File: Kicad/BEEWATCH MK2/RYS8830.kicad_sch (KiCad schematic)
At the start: 30 parts, among them Q4 BSS138, Q5 BSS138, Q6 BSS138, Q7 BSS138, U6 LTC3549EDCB#TRMPBF, U7 RYS8830

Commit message: Schematic changes
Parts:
- removed Q4: BSS138, Package_TO_SOT_SMD:SOT-23, symbol Transistor_FET:BSS138
- removed R25: 10K, Resistor_SMD:R_0402_1005Metric, symbol Device:R
- removed U6: LTC3549EDCB#TRMPBF, SON50P300X200X80-7N-D, symbol LTC3549EDCB#TRMPBF:LTC3549EDCB#TRMPBF
- added IC1: LTC3549EDCB#TRMPBF, Package_DFN_QFN:DFN-6-1EP_3x2mm_P0.5mm_EP1.65x1.35mm, symbol LTC3549EDCB#TRMPBF:LTC3549EDCB#TRMPBF
- added Q4: DMG6968U, Package_TO_SOT_SMD:SOT-23, symbol Transistor_FET:DMG2302U
- added Q8: DMP1045U-7, Package_TO_SOT_SMD:SOT-23-3, symbol Project_Library:DMP1045U-7
- added R49: 0, Resistor_SMD:R_0402_1005Metric_Pad0.72x0.64mm_HandSolder, symbol Device:R_Small
- added R50: 10K, Resistor_SMD:R_0402_1005Metric_Pad0.72x0.64mm_HandSolder, symbol Device:R
- L3: footprint Inductor_SMD:L_0402_1005Metric -> Inductor_SMD:L_Cenker_CKCS3012
- R24: value K10K -> 10K; footprint Resistor_SMD:R_0402_1005Metric -> Resistor_SMD:R_0402_1005Metric_Pad0.72x0.64mm_HandSolder
- R26, R27, R28, R29, R30, R31, R32, R33, R34, R35, R36, R37, R38, R39, R41: footprint Resistor_SMD:R_0402_1005Metric -> Resistor_SMD:R_0402_1005Metric_Pad0.72x0.64mm_HandSolder
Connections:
- net +1V8: now also R24.2, Q8.2 (S); no longer Q5.1 (G), Q6.1 (G), Q7.1 (G), R31.2, R32.2, R33.2, R41.2, U7.14 (SYSTEM0)
- net +3V3: no longer R24.2
- net GND: now also IC1.2 (GND_1), IC1.4 (MODE), IC1.7 (GND_2), Q4.2 (S), R50.1
- net GNSS_+1.8V: now also IC1.1 (VIN), IC1.5 (RUN)
- net GPS_EN: now also Q4.1 (G), R50.2; no longer R24.1
- net at C28.1, C29.2, L3.2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: now also R49.1; no longer U7.5 (LDO_IN)
- net at L3.1: now also IC1.3 (SW)
- net at C28.2, R26.2, R27.1: now also IC1.6 (VFB)
- new net: R49.2, U7.5 (LDO_IN)
- new net: Q4.3 (D), Q8.1 (G), R24.1
- new net GNSS_+1V8: Q5.1 (G), Q6.1 (G), Q7.1 (G), Q8.3 (D), R31.2, R32.2, R33.2, R41.2, U7.14 (SYSTEM0)

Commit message: GNSS level shifter floating voltage needs to be fix
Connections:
- net GNSS_+1.8V: now also Q5.1 (G), Q6.1 (G), Q7.1 (G), R31.2, R32.2, R33.2, U7.14 (SYSTEM0)
- net GNSS_+1V8: no longer Q5.1 (G), Q6.1 (G), Q7.1 (G), R31.2, R32.2, R33.2, U7.14 (SYSTEM0)

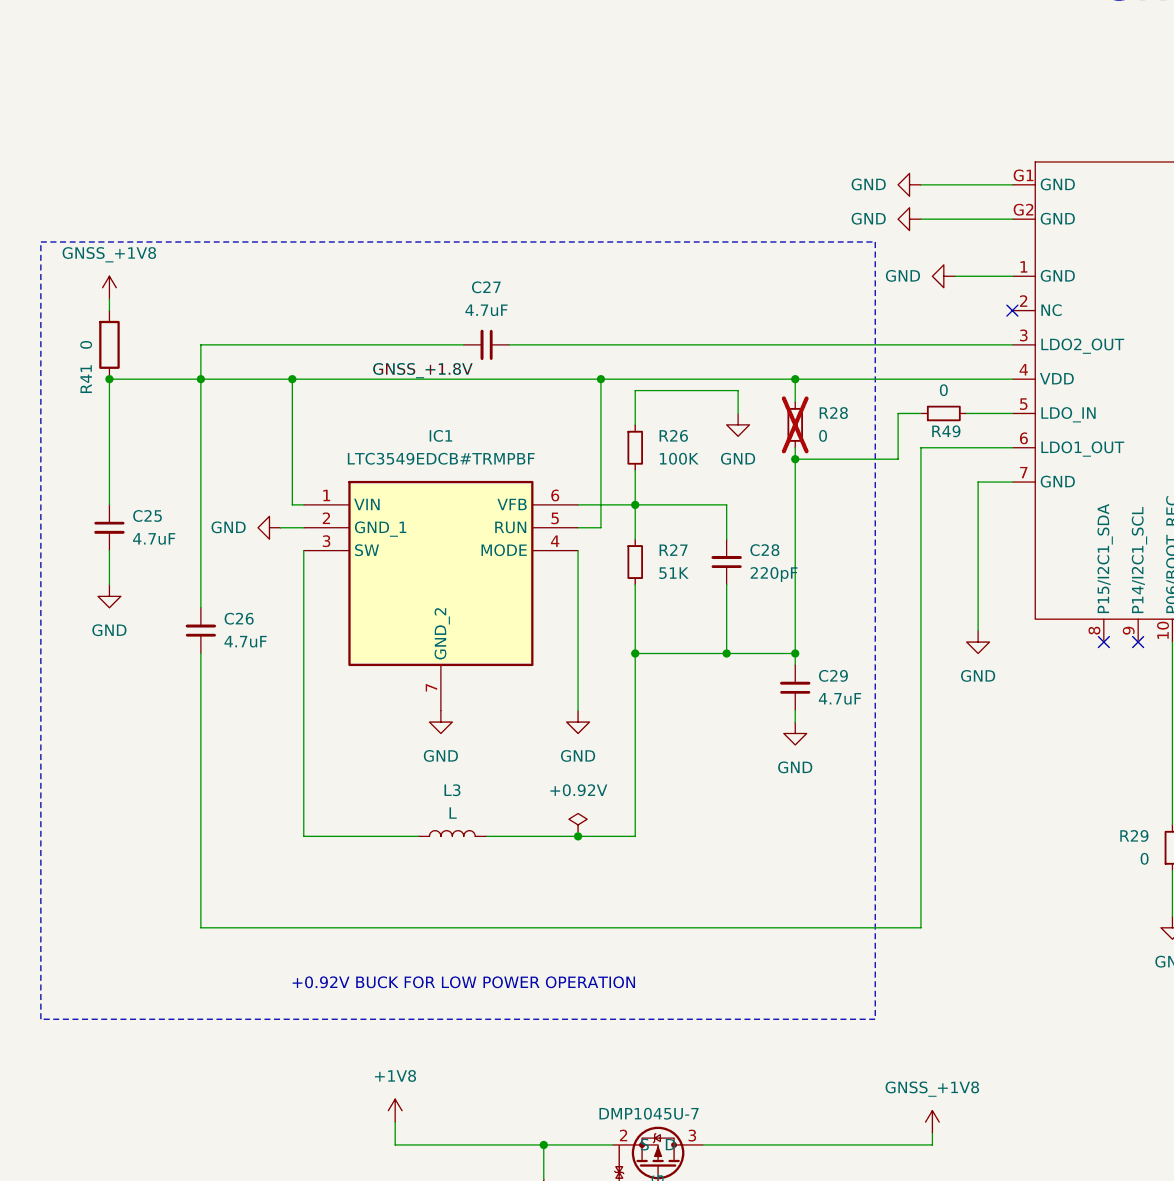
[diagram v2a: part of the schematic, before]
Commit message: Added Buzzer flyback diode
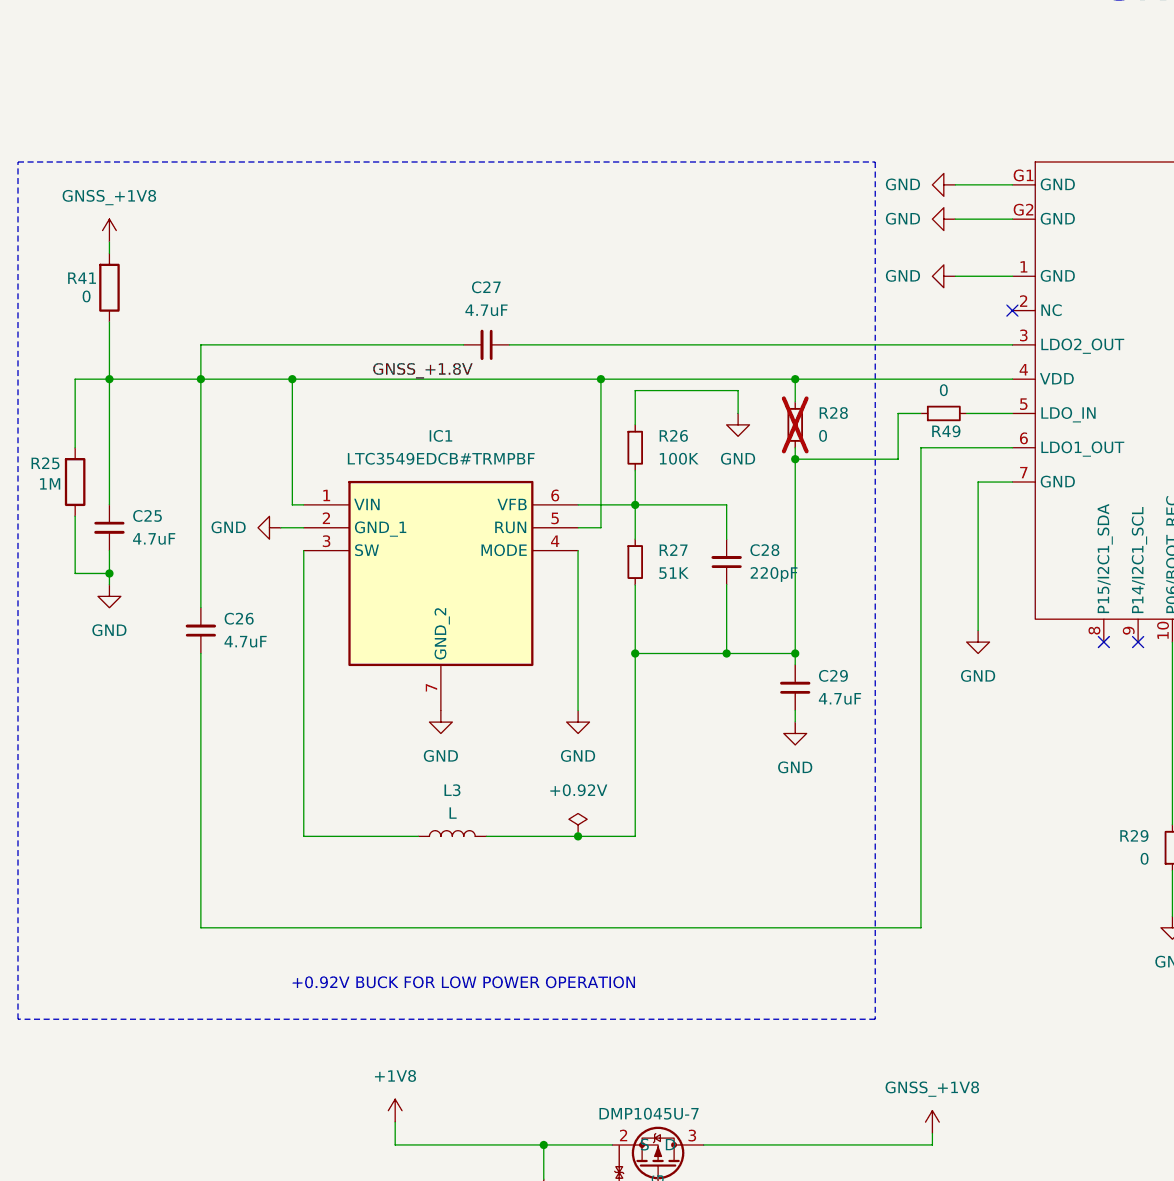
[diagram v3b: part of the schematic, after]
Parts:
- added R25: 1M, Resistor_SMD:R_0402_1005Metric_Pad0.72x0.64mm_HandSolder, symbol Device:R
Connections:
- net GND: now also R25.1
- net GNSS_+1.8V: now also R25.2
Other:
- moved on the sheet: R41
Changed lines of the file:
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@@
 	)
 	(junction
+		(at 30.48 90.17)
+		(diameter 0)
+		(color 0 0 0 0)
+	)
+	(junction
 		(at 228.6 83.82)
 		(diameter 0)
@@
 	(wire
 		(pts
-			(xy 30.48 87.63) (xy 30.48 91.44)
+			(xy 30.48 87.63) (xy 30.48 90.17)
 		)
 		(stroke
@@
 	(wire
 		(pts
+			(xy 26.67 76.2) (xy 26.67 68.58)
+		)
+		(stroke
+			(width 0)
+			(type default)
+		)
+	)
+	(wire
+		(pts
 			(xy 82.55 87.63) (xy 82.55 105.41)
 		)
@@
 	(wire
 		(pts
-			(xy 30.48 59.69) (xy 30.48 60.96)
+			(xy 30.48 53.34) (xy 30.48 54.61)
 		)
 		(stroke
@@
 	(wire
 		(pts
+			(xy 26.67 68.58) (xy 30.48 68.58)
+		)
+		(stroke
+			(width 0)
+			(type default)
+		)
+	)
+	(wire
+		(pts
 			(xy 241.3 59.69) (xy 247.65 59.69)
 		)
@@
 	(wire
 		(pts
+			(xy 26.67 90.17) (xy 30.48 90.17)
+		)
+		(stroke
+			(width 0)
+			(type default)
+		)
+	)
+	(wire
+		(pts
 			(xy 163.83 97.79) (xy 163.83 104.14)
 		)
@@
 	(wire
 		(pts
-			(xy 120.65 46.99) (xy 130.81 46.99)
+			(xy 124.46 46.99) (xy 130.81 46.99)
 		)
 		(stroke
@@
 	(wire
 		(pts
+			(xy 30.48 90.17) (xy 30.48 91.44)
+		)
+		(stroke
+			(width 0)
+			(type default)
+		)
+	)
+	(wire
+		(pts
 			(xy 88.9 78.74) (xy 88.9 82.55)
 		)
@@
 	(wire
 		(pts
-			(xy 120.65 50.8) (xy 130.81 50.8)
+			(xy 124.46 50.8) (xy 130.81 50.8)
 		)
 		(stroke
@@
 	(wire
 		(pts
+			(xy 26.67 83.82) (xy 26.67 90.17)
+		)
+		(stroke
+			(width 0)
+			(type default)
+		)
+	)
+	(wire
+		(pts
 			(xy 40.64 129.54) (xy 40.64 99.06)
 		)
@@
 	(wire
 		(pts
+			(xy 30.48 62.23) (xy 30.48 68.58)
+		)
+		(stroke
+			(width 0)
+			(type default)
+		)
+	)
+	(wire
+		(pts
 			(xy 40.64 64.77) (xy 40.64 68.58)
 		)
@@
 	)
 	(rectangle
-		(start 22.86 53.34)
+		(start 20.32 44.45)
 		(end 115.57 139.7)
 		(stroke
@@
 	(symbol
 		(lib_id "Device:R")
-		(at 30.48 64.77 0)
+		(at 30.48 58.42 0)
 		(mirror x)
 		(unit 1)
@@
 		(dnp no)
 		(property "Reference" "R41"
-			(at 27.94 68.58 90)
+			(at 27.432 57.404 0)
 			(effects
 				(font
@@
 		)
 		(property "Value" "0"
-			(at 27.94 64.77 90)
+			(at 27.94 59.436 0)
 			(effects
 				(font
@@
 		)
 		(property "Footprint" "Resistor_SMD:R_0402_1005Metric_Pad0.72x0.64mm_HandSolder"
-			(at 28.702 64.77 90)
+			(at 28.702 58.42 90)
 			(effects
 				(font
@@
 		)
 		(property "Datasheet" "~"
-			(at 30.48 64.77 0)
+			(at 30.48 58.42 0)
 			(effects
 				(font
@@
 		)
 		(property "Description" "Resistor"
-			(at 30.48 64.77 0)
+			(at 30.48 58.42 0)
 			(effects
 				(font
@@
 	)
 	(symbol
+		(lib_id "Device:R")
+		(at 26.67 80.01 0)
+		(mirror x)
+		(unit 1)
+		(exclude_from_sim no)
+		(in_bom yes)
+		(on_board yes)
+		(dnp no)
+		(property "Reference" "R25"
+			(at 23.368 77.978 0)
+			(effects
+				(font
+					(size 1.27 1.27)
+				)
+			)
+		)
+		(property "Value" "1M"
+			(at 23.876 80.264 0)
+			(effects
+				(font
+					(size 1.27 1.27)
+				)
+			)
+		)
+		(property "Footprint" "Resistor_SMD:R_0402_1005Metric_Pad0.72x0.64mm_HandSolder"
+			(at 24.892 80.01 90)
+			(effects
+				(font
+					(size 1.27 1.27)
+				)
+				(hide yes)
+			)
+		)
+		(property "Datasheet" "~"
+			(at 26.67 80.01 0)
+			(effects
+				(font
+					(size 1.27 1.27)
+				)
+				(hide yes)
+			)
+		)
+		(property "Description" "Resistor"
+			(at 26.67 80.01 0)
+			(effects
+				(font
+					(size 1.27 1.27)
+				)
+				(hide yes)
+			)
+		)
+		(pin "1"
+		)
+		(pin "2"
+		)
+		(instances
+			(project "BEEWATCH MK3"
+				(path "/e9c5fb53-480b-4989-8495-a3341ee99514/33dec73c-f7ec-4dd7-9d85-ef473e07baa9"
+					(reference "R25")
+					(unit 1)
+				)
+			)
+		)
+	)
+	(symbol
 		(lib_id "power:GND")
-		(at 120.65 46.99 270)
+		(at 124.46 46.99 270)
 		(unit 1)
 		(exclude_from_sim no)
@@
 		(fields_autoplaced yes)
 		(property "Reference" "#PWR053"
-			(at 114.3 46.99 0)
+			(at 118.11 46.99 0)
 			(effects
 				(font
@@
 		)
 		(property "Value" "GND"
-			(at 116.84 46.9899 90)
+			(at 120.65 46.9899 90)
 			(effects
 				(font
@@
 		)
 		(property "Footprint" ""
-			(at 120.65 46.99 0)
+			(at 124.46 46.99 0)
 			(effects
 				(font
@@
 		)
 		(property "Datasheet" ""
-			(at 120.65 46.99 0)
+			(at 124.46 46.99 0)
 			(effects
 				(font
@@
 		)
 		(property "Description" "Power symbol creates a global label with name \"GND\" , ground"
-			(at 120.65 46.99 0)
+			(at 124.46 46.99 0)
 			(effects
 				(font
@@
 	(symbol
 		(lib_id "power:+3.3V")
-		(at 30.48 59.69 0)
+		(at 30.48 53.34 0)
 		(mirror y)
 		(unit 1)
@@
 		(fields_autoplaced yes)
 		(property "Reference" "#PWR047"
-			(at 30.48 63.5 0)
+			(at 30.48 57.15 0)
 			(effects
 				(font
@@
 		)
 		(property "Value" "GNSS_+1V8"
-			(at 30.48 54.61 0)
+			(at 30.48 48.26 0)
 			(effects
 				(font
@@
 		)
 		(property "Footprint" ""
-			(at 30.48 59.69 0)
+			(at 30.48 53.34 0)
 			(effects
 				(font
@@
 		)
 		(property "Datasheet" ""
-			(at 30.48 59.69 0)
+			(at 30.48 53.34 0)
 			(effects
 				(font
@@
 		)
 		(property "Description" "Power symbol creates a global label with name \"+3.3V\""
-			(at 30.48 59.69 0)
+			(at 30.48 53.34 0)
 			(effects
 				(font
@@
 	(symbol
 		(lib_id "power:GND")
-		(at 120.65 50.8 270)
+		(at 124.46 50.8 270)
 		(unit 1)
 		(exclude_from_sim no)
@@
 		(fields_autoplaced yes)
 		(property "Reference" "#PWR054"
-			(at 114.3 50.8 0)
+			(at 118.11 50.8 0)
 			(effects
 				(font
@@
 		)
 		(property "Value" "GND"
-			(at 116.84 50.7999 90)
+			(at 120.65 50.7999 90)
 			(effects
 				(font
@@
 		)
 		(property "Footprint" ""
-			(at 120.65 50.8 0)
+			(at 124.46 50.8 0)
 			(effects
 				(font
@@
 		)
 		(property "Datasheet" ""
-			(at 120.65 50.8 0)
+			(at 124.46 50.8 0)
 			(effects
 				(font
@@
 		)
 		(property "Description" "Power symbol creates a global label with name \"GND\" , ground"
-			(at 120.65 50.8 0)
+			(at 124.46 50.8 0)
 			(effects
 				(font

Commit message: Updated with sub module lib
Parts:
- U7: footprint Project:RYS8830 -> REYAS:RYS8830
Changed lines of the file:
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@@
 			)
 		)
-		(property "Footprint" "Project:RYS8830"
+		(property "Footprint" "REYAS:RYS8830"
 			(at 133.35 46.99 0)
 			(effects

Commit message: ERC Checking
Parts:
- R34: value K10K -> 10K
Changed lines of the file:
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@@
 		(dnp no)
 		(property "Reference" "R34"
-			(at 231.14 57.15 90)
+			(at 231.14 56.642 90)
 			(effects
 				(font
@@
 			)
 		)
-		(property "Value" "K10K"
-			(at 231.14 53.34 90)
+		(property "Value" "10K"
+			(at 231.394 50.8 90)
 			(effects
 				(font
